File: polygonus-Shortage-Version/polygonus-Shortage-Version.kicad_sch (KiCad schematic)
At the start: 14 parts, among them J105 Conn_01x01, J107 Conn_01x01, J108 Conn_01x01, J3 Conn_01x32, J5 Conn_01x32, J6 Conn_01x16, J7 Conn_01x16

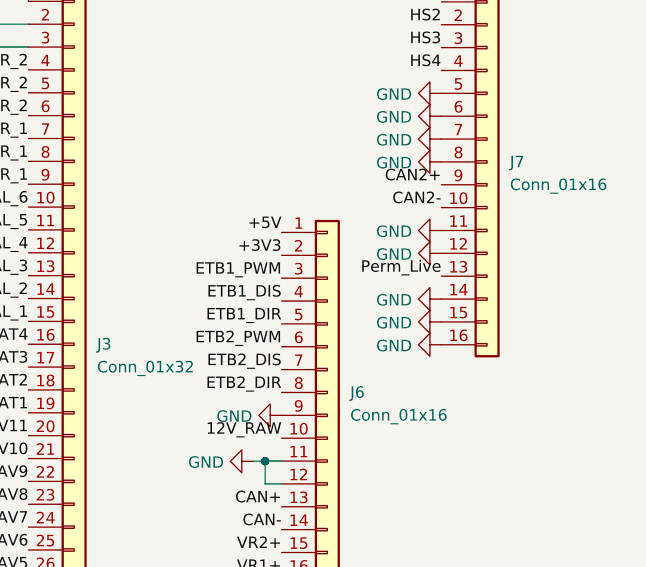
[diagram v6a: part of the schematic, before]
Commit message: Added 5x RSVD reserved pins for later
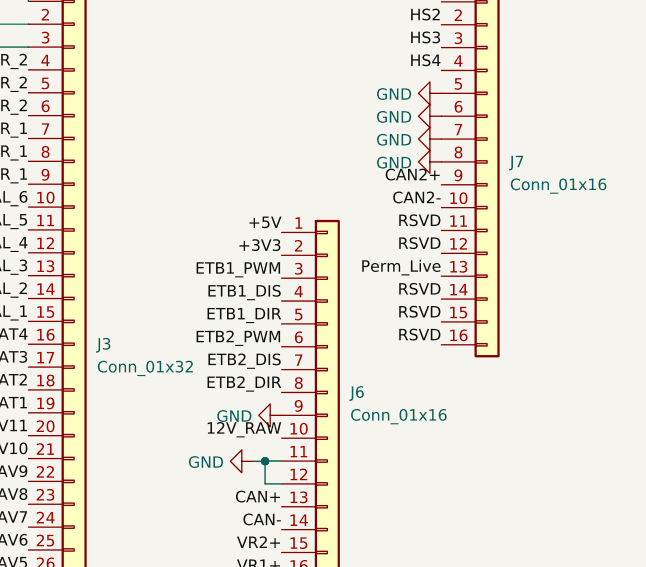
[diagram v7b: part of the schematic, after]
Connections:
- net GND: no longer J7.11 (Pin_11), J7.12 (Pin_12), J7.14 (Pin_14), J7.15 (Pin_15), J7.16 (Pin_16)
- new net RSVD: J7.11 (Pin_11), J7.12 (Pin_12), J7.14 (Pin_14), J7.15 (Pin_15), J7.16 (Pin_16)
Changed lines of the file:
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@@
+    (effects (font (size 1.27 1.27)) (justify right bottom))
+  )
+  (label "RSVD" (at 273.2114 52.1319 180)
     (effects (font (size 1.27 1.27)) (justify right bottom))
   )
@@
     (effects (font (size 1.27 1.27)) (justify right bottom))
   )
+  (label "RSVD" (at 273.2114 57.2119 180)
+    (effects (font (size 1.27 1.27)) (justify right bottom))
+  )
   (label "ETB2_DIS" (at 255.4645 65.0496 180)
     (effects (font (size 1.27 1.27)) (justify right bottom))
@@
     (effects (font (size 1.27 1.27)) (justify right bottom))
   )
+  (label "RSVD" (at 273.2114 49.5919 180)
+    (effects (font (size 1.27 1.27)) (justify right bottom))
+  )
   (label "12V_RAW" (at 255.4645 72.6696 180)
     (effects (font (size 1.27 1.27)) (justify right bottom))
@@
     (effects (font (size 1.27 1.27)) (justify right bottom))
   )
+  (label "RSVD" (at 273.2114 62.2919 180)
+    (effects (font (size 1.27 1.27)) (justify right bottom))
+  )
   (label "LS6" (at 140.97 37.465 0)
     (effects (font (size 1.27 1.27)) (justify left bottom))
@@
   (label "LS14" (at 140.97 69.215 0)
     (effects (font (size 1.27 1.27)) (justify left bottom))
+  )
+  (label "RSVD" (at 273.2114 59.7519 180)
+    (effects (font (size 1.27 1.27)) (justify right bottom))
   )
   (label "HS4" (at 273.2114 31.8119 180)
@@
     (pin "1")
   )
-  (symbol (lib_id "power:GND") (at 273.2114 57.2119 270) (unit 1)
-    (in_bom yes) (on_board yes)
-    (property "Reference" "#PWR0151" (id 0) (at 266.8614 57.2119 0)
-      (effects (font (size 1.27 1.27)) hide)
-    )
-    (property "Value" "GND" (id 1) (at 269.9602 57.3389 90)
-      (effects (font (size 1.27 1.27)) (justify right))
-    )
-    (property "Footprint" "" (id 2) (at 273.2114 57.2119 0)
-      (effects (font (size 1.27 1.27)) hide)
-    )
-    (property "Datasheet" "" (id 3) (at 273.2114 57.2119 0)
-      (effects (font (size 1.27 1.27)) hide)
-    )
-    (pin "1")
-  )
   (symbol (lib_id "power:GND") (at 195.58 26.67 270) (unit 1)
     (in_bom yes) (on_board yes)
@@
     )
     (property "Datasheet" "" (id 3) (at 195.58 26.67 0)
-      (effects (font (size 1.27 1.27)) hide)
-    )
-    (pin "1")
-  )
-  (symbol (lib_id "power:GND") (at 273.2114 49.5919 270) (unit 1)
-    (in_bom yes) (on_board yes)
-    (property "Reference" "#PWR0152" (id 0) (at 266.8614 49.5919 0)
-      (effects (font (size 1.27 1.27)) hide)
-    )
-    (property "Value" "GND" (id 1) (at 269.9602 49.7189 90)
-      (effects (font (size 1.27 1.27)) (justify right))
-    )
-    (property "Footprint" "" (id 2) (at 273.2114 49.5919 0)
-      (effects (font (size 1.27 1.27)) hide)
-    )
-    (property "Datasheet" "" (id 3) (at 273.2114 49.5919 0)
       (effects (font (size 1.27 1.27)) hide)
     )
@@
     (pin "9")
   )
-  (symbol (lib_id "power:GND") (at 273.2114 59.7519 270) (unit 1)
-    (in_bom yes) (on_board yes)
-    (property "Reference" "#PWR0150" (id 0) (at 266.8614 59.7519 0)
-      (effects (font (size 1.27 1.27)) hide)
-    )
-    (property "Value" "GND" (id 1) (at 269.9602 59.8789 90)
-      (effects (font (size 1.27 1.27)) (justify right))
-    )
-    (property "Footprint" "" (id 2) (at 273.2114 59.7519 0)
-      (effects (font (size 1.27 1.27)) hide)
-    )
-    (property "Datasheet" "" (id 3) (at 273.2114 59.7519 0)
-      (effects (font (size 1.27 1.27)) hide)
-    )
-    (pin "1")
-  )
-  (symbol (lib_id "power:GND") (at 273.2114 62.2919 270) (unit 1)
-    (in_bom yes) (on_board yes)
-    (property "Reference" "#PWR0145" (id 0) (at 266.8614 62.2919 0)
-      (effects (font (size 1.27 1.27)) hide)
-    )
-    (property "Value" "GND" (id 1) (at 269.9602 62.4189 90)
-      (effects (font (size 1.27 1.27)) (justify right))
-    )
-    (property "Footprint" "" (id 2) (at 273.2114 62.2919 0)
-      (effects (font (size 1.27 1.27)) hide)
-    )
-    (property "Datasheet" "" (id 3) (at 273.2114 62.2919 0)
-      (effects (font (size 1.27 1.27)) hide)
-    )
-    (pin "1")
-  )
-  (symbol (lib_id "power:GND") (at 273.2114 52.1319 270) (unit 1)
-    (in_bom yes) (on_board yes)
-    (property "Reference" "#PWR0146" (id 0) (at 266.8614 52.1319 0)
-      (effects (font (size 1.27 1.27)) hide)
-    )
-    (property "Value" "GND" (id 1) (at 269.9602 52.2589 90)
-      (effects (font (size 1.27 1.27)) (justify right))
-    )
-    (property "Footprint" "" (id 2) (at 273.2114 52.1319 0)
-      (effects (font (size 1.27 1.27)) hide)
-    )
-    (property "Datasheet" "" (id 3) (at 273.2114 52.1319 0)
-      (effects (font (size 1.27 1.27)) hide)
-    )
-    (pin "1")
-  )
   (symbol (lib_id "Connector_Generic:Conn_01x16") (at 260.5445 67.5896 0) (unit 1)
     (in_bom yes) (on_board yes) (fields_autoplaced)
@@
       (reference "#PWR0144") (unit 1) (value "GND") (footprint "")
     )
-    (path "/b5338ae2-d647-48e4-a4ab-563fe2a0f01e"
-      (reference "#PWR0145") (unit 1) (value "GND") (footprint "")
-    )
-    (path "/dac98d69-2e36-4c84-8ac1-72fa28cfa676"
-      (reference "#PWR0146") (unit 1) (value "GND") (footprint "")
-    )
     (path "/00000000-0000-0000-0000-00005d98a146/85b0c444-48f2-41ee-b642-b6821afa6059"
       (reference "#PWR0148") (unit 1) (value "GND") (footprint "")
@@
       (reference "#PWR0149") (unit 1) (value "GND") (footprint "")
     )
-    (path "/b5285483-a615-4951-bbb5-5b4452874428"
-      (reference "#PWR0150") (unit 1) (value "GND") (footprint "")
-    )
-    (path "/017d7d87-577e-4f0d-9afe-caf967cfe679"
-      (reference "#PWR0151") (unit 1) (value "GND") (footprint "")
-    )
-    (path "/78390e5d-285f-450d-b452-56b6be5d8773"
-      (reference "#PWR0152") (unit 1) (value "GND") (footprint "")
-    )
     (path "/00000000-0000-0000-0000-00005da72eff/e63afe82-cb97-4952-a3a3-7a53a0ec5bcd"

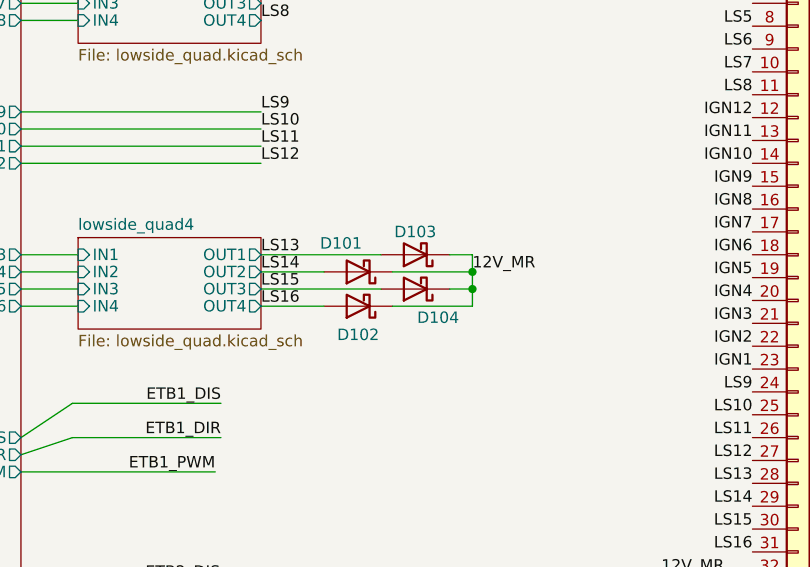
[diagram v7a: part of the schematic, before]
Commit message: removed diodes, need to do cleanup
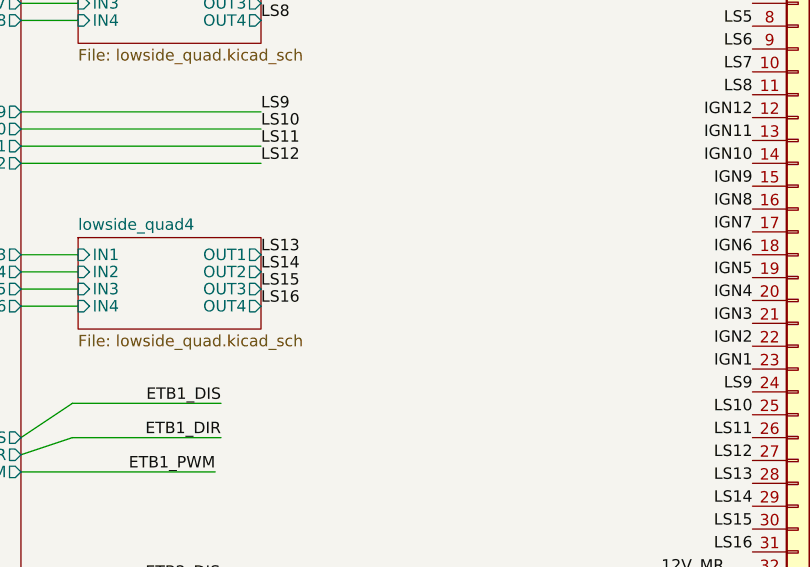
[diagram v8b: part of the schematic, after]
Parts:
- removed D101, D102, D103, D104: D_Schottky, Diode_SMD:D_SMA, symbol Device:D_Schottky
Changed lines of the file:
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@@
     (comment 2 "rusefi.com/s/proteus")
   )
-  (junction (at 164.465 69.215) (diameter 0) (color 0 0 0 0)
-  )
-  (junction (at 164.465 71.12) (diameter 0) (color 0 0 0 0)
-  )
   (junction (at 253.6325 75.2096) (diameter 0) (color 0 0 0 0)
   )
@@
     (stroke (width 0) (type default) (color 0 0 0 0))
   )
-  (wire (pts (xy 147.955 69.215) (xy 140.97 69.215))
-    (stroke (width 0) (type default) (color 0 0 0 0))
-  )
-  (wire (pts (xy 164.465 69.215) (xy 164.465 67.31))
-    (stroke (width 0) (type default) (color 0 0 0 0))
-  )
   (wire (pts (xy 123.825 142.875) (xy 114.3 142.875))
     (stroke (width 0) (type default) (color 0 0 0 0))
@@
     (stroke (width 0) (type default) (color 0 0 0 0))
   )
-  (wire (pts (xy 140.97 67.31) (xy 154.305 67.31))
-    (stroke (width 0) (type default) (color 0 0 0 0))
-  )
   (wire (pts (xy 120.65 73.025) (xy 114.3 73.025))
     (stroke (width 0) (type default) (color 0 0 0 0))
@@
     (stroke (width 0) (type default) (color 0 0 0 0))
   )
-  (wire (pts (xy 140.97 71.12) (xy 154.305 71.12))
-    (stroke (width 0) (type default) (color 0 0 0 0))
-  )
   (wire (pts (xy 120.015 106.68) (xy 114.3 107.315))
     (stroke (width 0) (type default) (color 0 0 0 0))
@@
     (stroke (width 0) (type default) (color 0 0 0 0))
   )
-  (wire (pts (xy 147.955 73.025) (xy 140.97 73.025))
-    (stroke (width 0) (type default) (color 0 0 0 0))
-  )
-  (wire (pts (xy 164.465 67.31) (xy 161.925 67.31))
-    (stroke (width 0) (type default) (color 0 0 0 0))
-  )
   (wire (pts (xy 114.3 55.245) (xy 140.97 55.245))
     (stroke (width 0) (type default) (color 0 0 0 0))
@@
     (stroke (width 0) (type default) (color 0 0 0 0))
   )
-  (wire (pts (xy 161.925 71.12) (xy 164.465 71.12))
-    (stroke (width 0) (type default) (color 0 0 0 0))
-  )
   (wire (pts (xy 205.74 14.7786) (xy 205.74 29.21))
     (stroke (width 0) (type default) (color 0 0 0 0))
@@
     (stroke (width 0) (type default) (color 0 0 0 0))
   )
-  (wire (pts (xy 164.465 73.025) (xy 164.465 71.12))
-    (stroke (width 0) (type default) (color 0 0 0 0))
-  )
   (wire (pts (xy 123.825 126.365) (xy 114.3 126.365))
     (stroke (width 0) (type default) (color 0 0 0 0))
@@
     (stroke (width 0) (type default) (color 0 0 0 0))
   )
-  (wire (pts (xy 155.575 73.025) (xy 164.465 73.025))
-    (stroke (width 0) (type default) (color 0 0 0 0))
-  )
   (wire (pts (xy 68.58 83.185) (xy 59.055 83.185))
     (stroke (width 0) (type default) (color 0 0 0 0))
@@
     (stroke (width 0) (type default) (color 0 0 0 0))
   )
-  (wire (pts (xy 164.465 69.215) (xy 155.575 69.215))
-    (stroke (width 0) (type default) (color 0 0 0 0))
-  )
   (wire (pts (xy 114.3 57.15) (xy 140.97 57.15))
     (stroke (width 0) (type default) (color 0 0 0 0))
@@
     (stroke (width 0) (type default) (color 0 0 0 0))
   )
-  (wire (pts (xy 164.465 71.12) (xy 164.465 69.215))
-    (stroke (width 0) (type default) (color 0 0 0 0))
-  )
   (wire (pts (xy 120.015 87.63) (xy 114.3 89.535))
     (stroke (width 0) (type default) (color 0 0 0 0))
@@
     (effects (font (size 1.27 1.27)) (justify left bottom))
   )
-  (label "12V_MR" (at 164.465 69.215 0)
-    (effects (font (size 1.27 1.27)) (justify left bottom))
-  )
   (label "LS3" (at 195.58 36.83 180)
     (effects (font (size 1.27 1.27)) (justify right bottom))
@@
     (pin "1")
   )
-  (symbol (lib_id "Device:D_Schottky") (at 151.765 73.025 180) (unit 1)
-    (in_bom yes) (on_board yes)
-    (property "Reference" "D102" (id 0) (at 151.765 76.2 0))
-    (property "Value" "D_Schottky" (id 1) (at 151.765 69.85 0)
-      (effects (font (size 1.27 1.27)) hide)
-    )
-    (property "Footprint" "Diode_SMD:D_SMA" (id 2) (at 151.765 73.025 0)
-      (effects (font (size 1.27 1.27)) hide)
-    )
-    (property "Datasheet" "~" (id 3) (at 151.765 73.025 0)
-      (effects (font (size 1.27 1.27)) hide)
-    )
-    (property "LCSC" "C8678" (id 4) (at 151.765 73.025 0)
-      (effects (font (size 1.27 1.27)) hide)
-    )
-    (property "LCSC_ext" "0" (id 5) (at 151.765 73.025 0)
-      (effects (font (size 1.27 1.27)) hide)
-    )
-    (pin "1")
-    (pin "2")
-  )
-  (symbol (lib_id "Device:D_Schottky") (at 158.115 71.12 180) (unit 1)
-    (in_bom yes) (on_board yes)
-    (property "Reference" "D104" (id 0) (at 160.655 74.295 0))
-    (property "Value" "D_Schottky" (id 1) (at 158.115 67.945 0)
-      (effects (font (size 1.27 1.27)) hide)
-    )
-    (property "Footprint" "Diode_SMD:D_SMA" (id 2) (at 158.115 71.12 0)
-      (effects (font (size 1.27 1.27)) hide)
-    )
-    (property "Datasheet" "~" (id 3) (at 158.115 71.12 0)
-      (effects (font (size 1.27 1.27)) hide)
-    )
-    (property "LCSC" "C8678" (id 4) (at 158.115 71.12 0)
-      (effects (font (size 1.27 1.27)) hide)
-    )
-    (property "LCSC_ext" "0" (id 5) (at 158.115 71.12 0)
-      (effects (font (size 1.27 1.27)) hide)
-    )
-    (pin "1")
-    (pin "2")
-  )
-  (symbol (lib_id "Device:D_Schottky") (at 151.765 69.215 180) (unit 1)
-    (in_bom yes) (on_board yes)
-    (property "Reference" "D101" (id 0) (at 149.86 66.04 0))
-    (property "Value" "D_Schottky" (id 1) (at 151.765 66.04 0)
-      (effects (font (size 1.27 1.27)) hide)
-    )
-    (property "Footprint" "Diode_SMD:D_SMA" (id 2) (at 151.765 69.215 0)
-      (effects (font (size 1.27 1.27)) hide)
-    )
-    (property "Datasheet" "~" (id 3) (at 151.765 69.215 0)
-      (effects (font (size 1.27 1.27)) hide)
-    )
-    (property "LCSC" "C8678" (id 4) (at 151.765 69.215 0)
-      (effects (font (size 1.27 1.27)) hide)
-    )
-    (property "LCSC_ext" "0" (id 5) (at 151.765 69.215 0)
-      (effects (font (size 1.27 1.27)) hide)
-    )
-    (pin "1")
-    (pin "2")
-  )
-  (symbol (lib_id "Device:D_Schottky") (at 158.115 67.31 180) (unit 1)
-    (in_bom yes) (on_board yes)
-    (property "Reference" "D103" (id 0) (at 158.115 64.77 0))
-    (property "Value" "D_Schottky" (id 1) (at 158.115 64.135 0)
-      (effects (font (size 1.27 1.27)) hide)
-    )
-    (property "Footprint" "Diode_SMD:D_SMA" (id 2) (at 158.115 67.31 0)
-      (effects (font (size 1.27 1.27)) hide)
-    )
-    (property "Datasheet" "~" (id 3) (at 158.115 67.31 0)
-      (effects (font (size 1.27 1.27)) hide)
-    )
-    (property "LCSC" "C8678" (id 4) (at 158.115 67.31 0)
-      (effects (font (size 1.27 1.27)) hide)
-    )
-    (property "LCSC_ext" "0" (id 5) (at 158.115 67.31 0)
-      (effects (font (size 1.27 1.27)) hide)
-    )
-    (pin "1")
-    (pin "2")
-  )
   (symbol (lib_id "Device:CP") (at 194.343 108.614 0) (unit 1)
     (in_bom yes) (on_board yes)
@@
       (reference "D7") (unit 1) (value "schottky") (footprint "Diode_SMD:D_SOD-123")
     )
-    (path "/00000000-0000-0000-0000-00005e988fe1"
-      (reference "D101") (unit 1) (value "D_Schottky") (footprint "Diode_SMD:D_SMA")
-    )
-    (path "/00000000-0000-0000-0000-00005e9878f9"
-      (reference "D102") (unit 1) (value "D_Schottky") (footprint "Diode_SMD:D_SMA")
-    )
-    (path "/00000000-0000-0000-0000-00005e9897d0"
-      (reference "D103") (unit 1) (value "D_Schottky") (footprint "Diode_SMD:D_SMA")
-    )
-    (path "/00000000-0000-0000-0000-00005e9888d3"
-      (reference "D104") (unit 1) (value "D_Schottky") (footprint "Diode_SMD:D_SMA")
-    )
     (path "/00000000-0000-0000-0000-00005da72eff/00000000-0000-0000-0000-00005e9d2c4f"
